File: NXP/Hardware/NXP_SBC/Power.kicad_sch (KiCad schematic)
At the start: 65 parts, among them Q1 DMN3150L-7, Q2 DMN3150L-7, Q3 DMN3150L-7, Q4 DMN3150L-7, Q5 DMN3150L-7, U3 AP3401, U4 AP3401, U5 MP2144GJ-P, U6 MAX811REUS-T

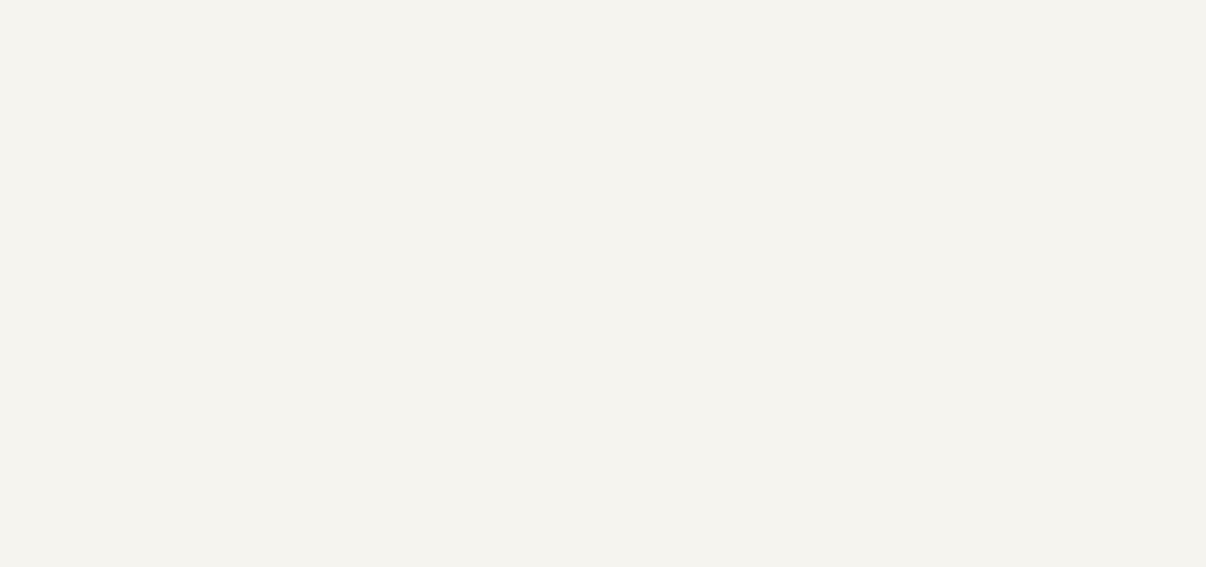
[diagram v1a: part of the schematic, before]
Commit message: Added more to ethernet schematic
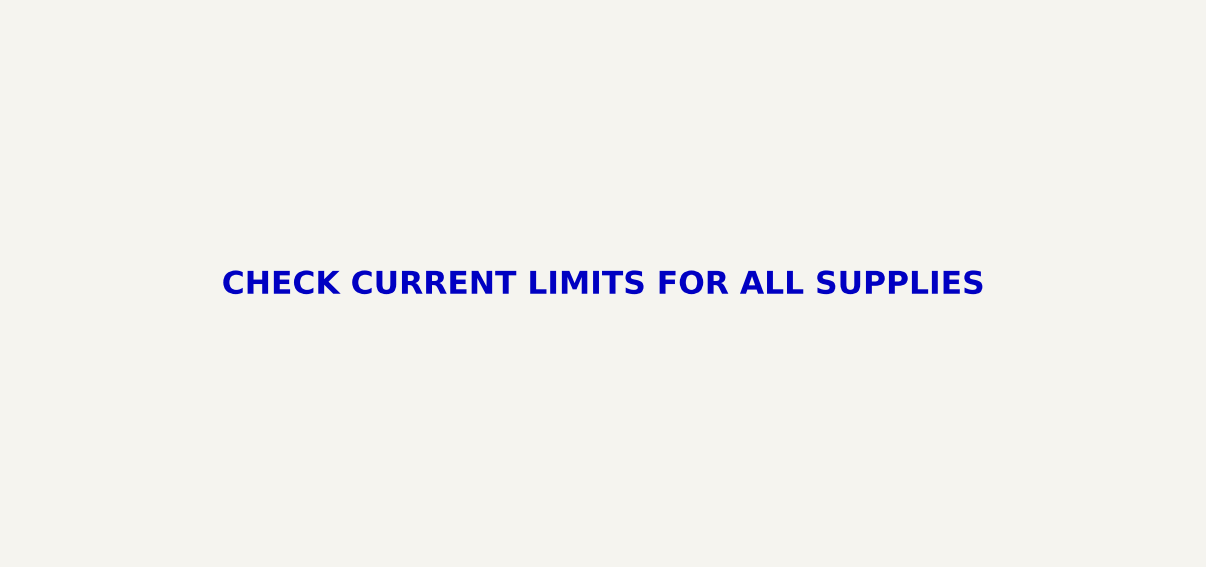
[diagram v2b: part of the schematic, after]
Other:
- note added: "CHECK CURRENT LIMITS FOR ALL SUPPLIES"
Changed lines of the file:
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@@
+		)
+	)
+	(text "CHECK CURRENT LIMITS FOR ALL SUPPLIES"
+		(exclude_from_sim no)
+		(at 196.596 302.514 0)
+		(effects
+			(font
+				(size 2.54 2.54)
+				(thickness 0.254)
+				(bold yes)
+				(color 255 0 0 1)
+			)
 		)
 	)

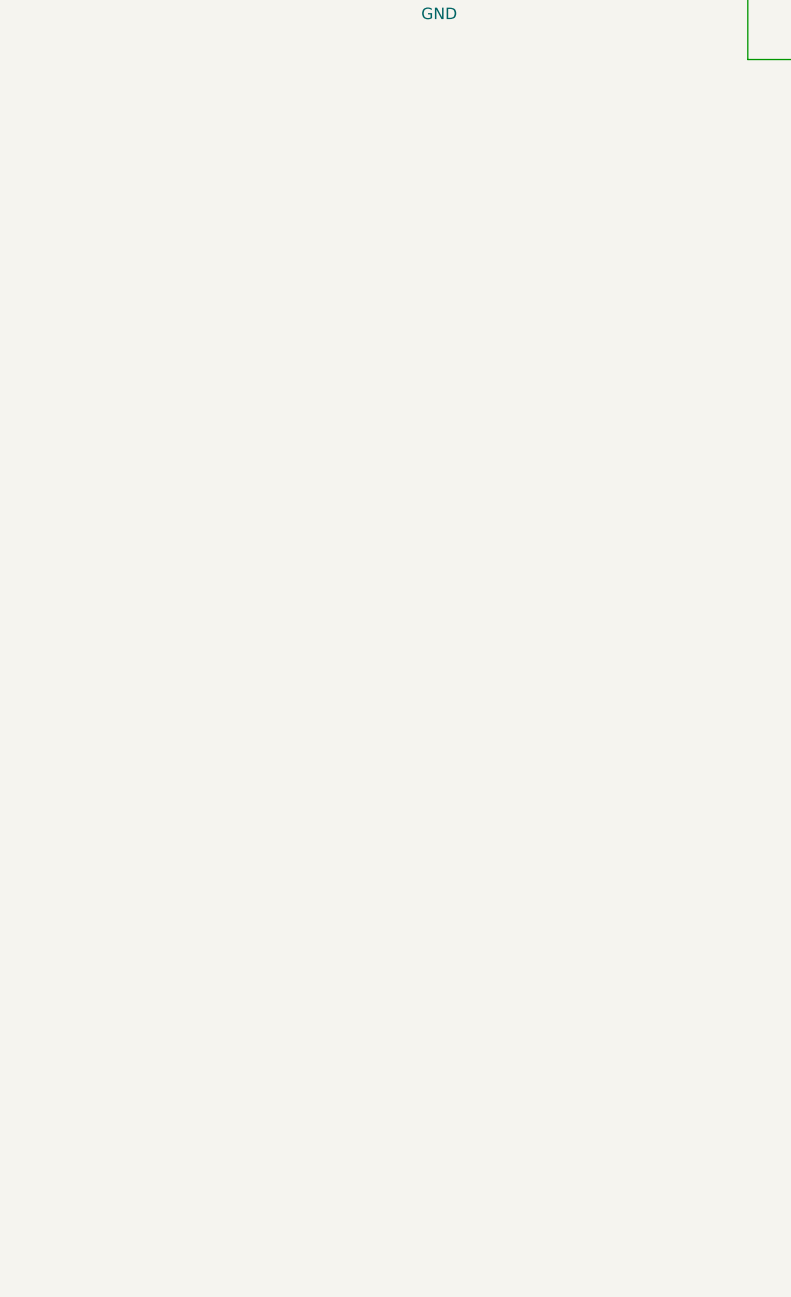
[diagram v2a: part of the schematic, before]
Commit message: added in Maya Wifi/BT module
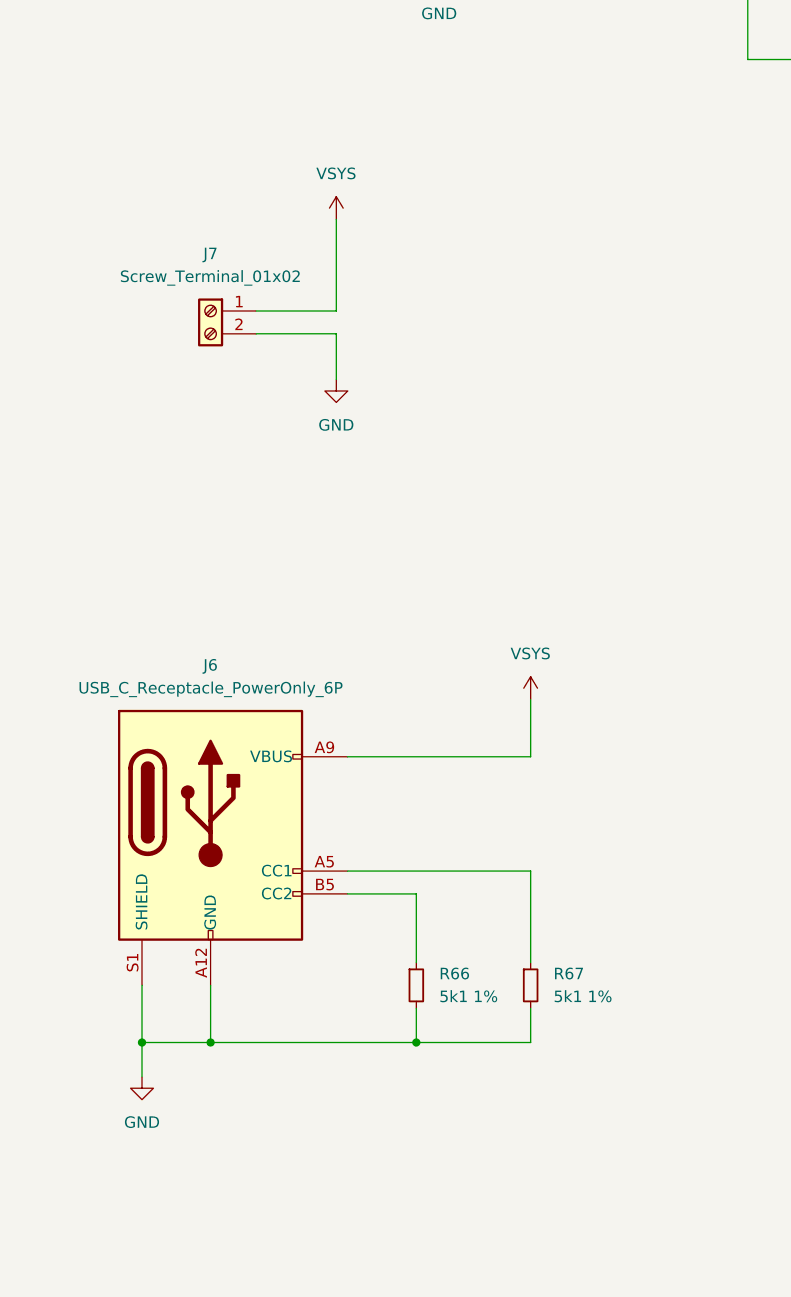
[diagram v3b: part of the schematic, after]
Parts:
- added J6: USB_C_Receptacle_PowerOnly_6P, Connector_USB:USB_C_Receptacle_GCT_USB4125-xx-x_6P_TopMnt_Horizontal, symbol Connector:USB_C_Receptacle_PowerOnly_6P
- added J7: Screw_Terminal_01x02, TerminalBlock_MetzConnect:TerminalBlock_MetzConnect_Type101_RT01602HBWC_1x02_P5.08mm_Horizontal, symbol Connector:Screw_Terminal_01x02
- added R66, R67: 5k1 1%, Resistor_SMD:R_0603_1608Metric, symbol Device:R_Small
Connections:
- net GND: now also J6.A12 (GND), J6.B12 (GND), J6.S1 (SHIELD), J7.2 (Pin_2), R66.2, R67.2
- net VSYS: now also J6.A9 (VBUS), J6.B9 (VBUS), J7.1 (Pin_1)
- new net: J6.B5 (CC2), R66.1
- new net: J6.A5 (CC1), R67.1

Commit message: More additions to schematic
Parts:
- added C61, C62: 10uF, Capacitor_SMD:C_0603_1608Metric_Pad1.08x0.95mm_HandSolder, symbol Device:C_Small
- added C63, C66: 100nF, Capacitor_SMD:C_0603_1608Metric_Pad1.08x0.95mm_HandSolder, symbol Device:C_Small
- added C64: 22pF, Capacitor_SMD:C_0603_1608Metric_Pad1.08x0.95mm_HandSolder, symbol Device:C_Small
- added C65: 22uF, Capacitor_SMD:C_0603_1608Metric_Pad1.08x0.95mm_HandSolder, symbol Device:C_Small
- added C67: 1nF, Capacitor_SMD:C_0603_1608Metric_Pad1.08x0.95mm_HandSolder, symbol Device:C_Small
- added L4: 2u2, Inductor_SMD:L_7.3x7.3_H3.5, symbol Device:L
- added Q6: DMN3150L-7, Package_TO_SOT_SMD:SOT-23, symbol Transistor_FET:DMN3150L
- added R68: 100k, Resistor_SMD:R_0603_1608Metric, symbol Device:R_Small
- added R69: 10k, Resistor_SMD:R_0603_1608Metric, symbol Device:R_Small
- added R70: 300k, 1%, Resistor_SMD:R_0603_1608Metric, symbol Device:R_Small
- added R71: 150k, 1%, Resistor_SMD:R_0603_1608Metric, symbol Device:R_Small
- added R72: 51R, Resistor_SMD:R_0603_1608Metric, symbol Device:R_Small
- added R73: 0R, Resistor_SMD:R_0603_1608Metric, symbol Device:R_Small
- added U9: AP3401, Package_TO_SOT_SMD:TSOT-23-6, symbol Regulator_Switching:AP3402
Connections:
- net DCDC_3V3: now also R69.1
- net DISCHG_EN: now also C67.1, Q6.1 (G)
- net GND: now also C61.2, C62.2, C63.2, C65.2, C66.2, C67.2, Q6.2 (S), R71.2, U9.2 (GND)
- net VSYS: now also C61.1, C62.1, C63.1, R68.1, U9.4 (VIN)
- new net: C64.2, R70.2, R71.1, U9.6 (FB)
- new net: L4.1, U9.3 (LX)
- new net: C64.1, C65.1, C66.1, L4.2, R70.1, R72.1, R73.1
- new net: R69.2, U9.1 (EN)
- new net: R68.2, U9.5 (PG)
- new net: Q6.3 (D), R72.2
- new net +1V8: R73.2
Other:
- moved on the sheet: J6, J7, R66, R67

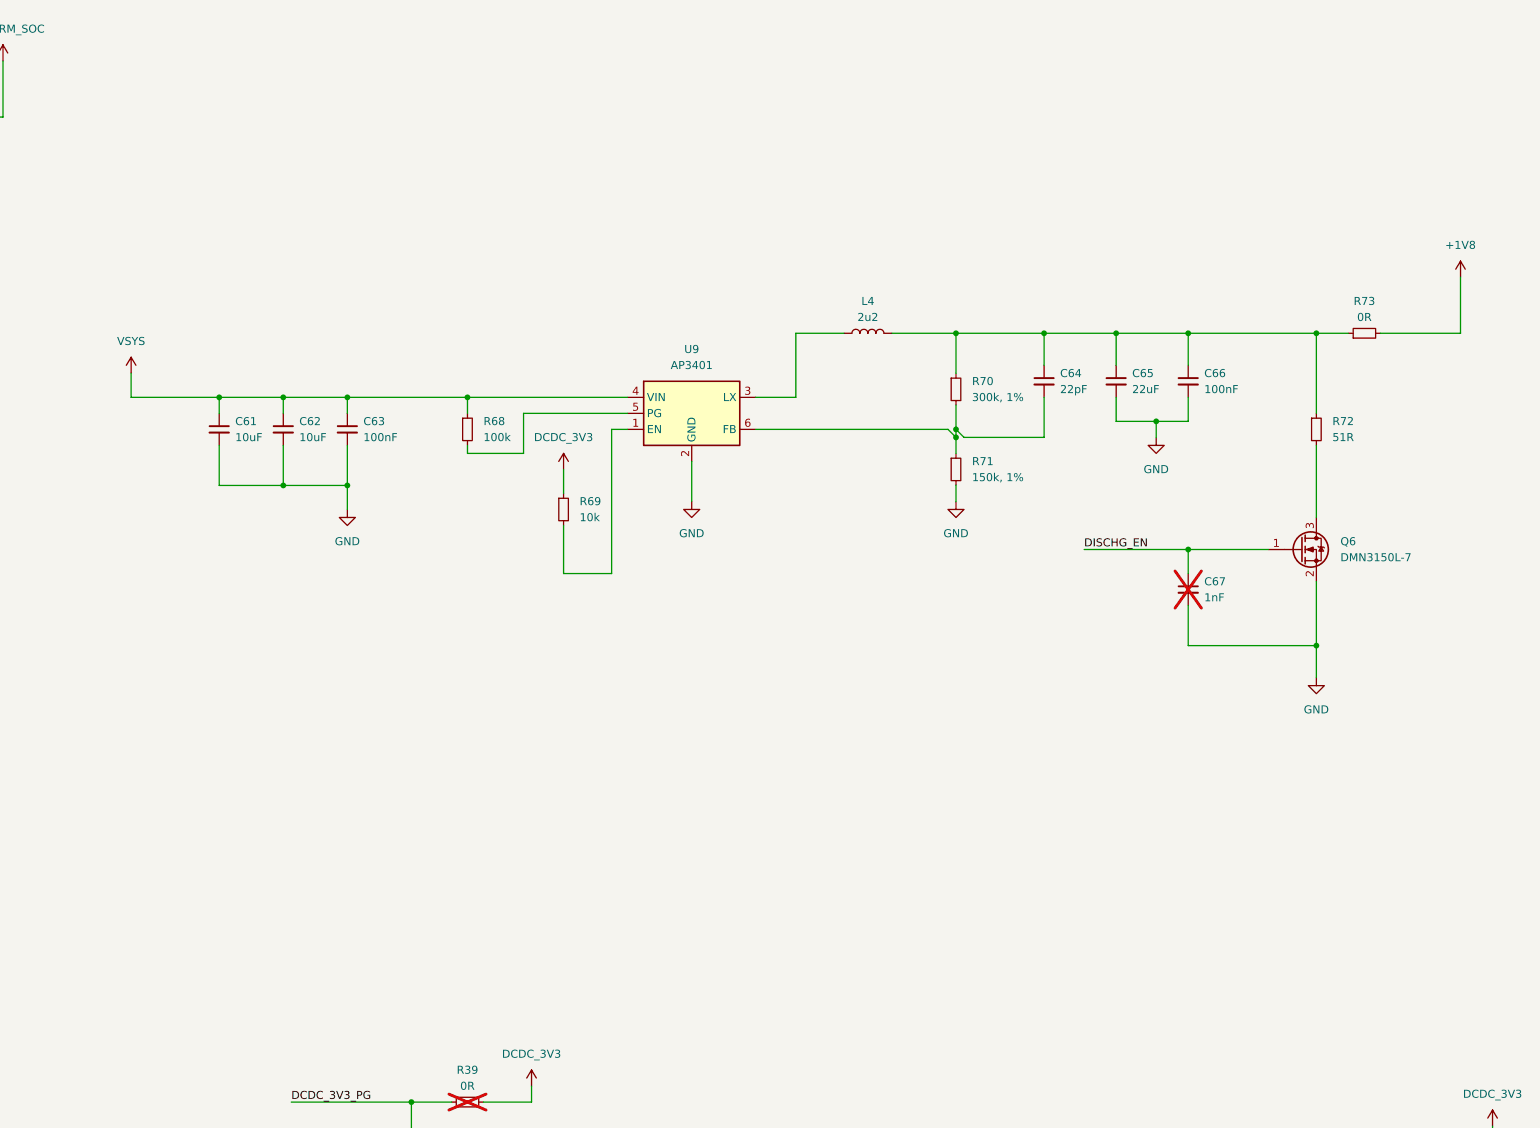
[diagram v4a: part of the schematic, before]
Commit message: Updates to radio connections
Also used the pin configurator tool to better understand pin mapping of the imx processor
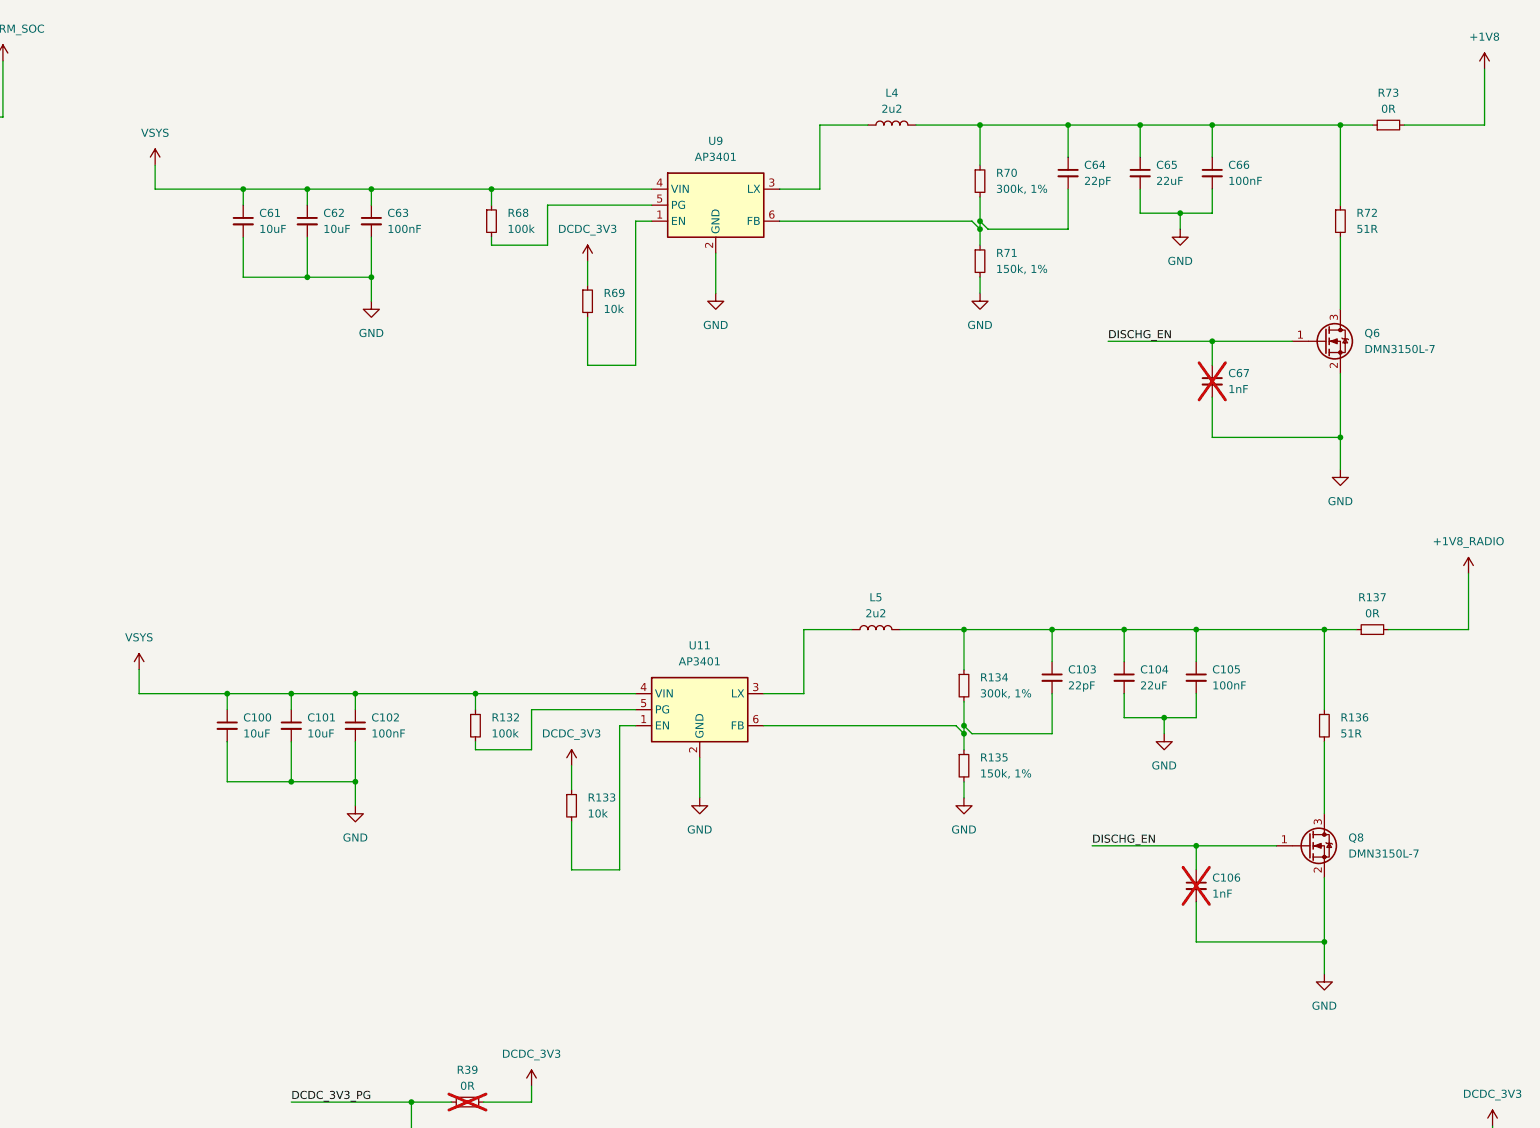
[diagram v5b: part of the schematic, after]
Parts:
- added C100, C101: 10uF, Capacitor_SMD:C_0603_1608Metric_Pad1.08x0.95mm_HandSolder, symbol Device:C_Small
- added C102, C105: 100nF, Capacitor_SMD:C_0603_1608Metric_Pad1.08x0.95mm_HandSolder, symbol Device:C_Small
- added C103: 22pF, Capacitor_SMD:C_0603_1608Metric_Pad1.08x0.95mm_HandSolder, symbol Device:C_Small
- added C104: 22uF, Capacitor_SMD:C_0603_1608Metric_Pad1.08x0.95mm_HandSolder, symbol Device:C_Small
- added C106: 1nF, Capacitor_SMD:C_0603_1608Metric_Pad1.08x0.95mm_HandSolder, symbol Device:C_Small
- added L5: 2u2, Inductor_SMD:L_7.3x7.3_H3.5, symbol Device:L
- added Q8: DMN3150L-7, Package_TO_SOT_SMD:SOT-23, symbol Transistor_FET:DMN3150L
- added R132: 100k, Resistor_SMD:R_0603_1608Metric, symbol Device:R_Small
- added R133: 10k, Resistor_SMD:R_0603_1608Metric, symbol Device:R_Small
- added R134: 300k, 1%, Resistor_SMD:R_0603_1608Metric, symbol Device:R_Small
- added R135: 150k, 1%, Resistor_SMD:R_0603_1608Metric, symbol Device:R_Small
- added R136: 51R, Resistor_SMD:R_0603_1608Metric, symbol Device:R_Small
- added R137: 0R, Resistor_SMD:R_0603_1608Metric, symbol Device:R_Small
- added U11: AP3401, Package_TO_SOT_SMD:TSOT-23-6, symbol Regulator_Switching:AP3402
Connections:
- net DCDC_3V3: now also R133.1
- net DISCHG_EN: now also C106.1, Q8.1 (G)
- net GND: now also C100.2, C101.2, C102.2, C104.2, C105.2, C106.2, Q8.2 (S), R135.2, U11.2 (GND)
- net VSYS: now also C100.1, C101.1, C102.1, R132.1, U11.4 (VIN)
- new net: C103.1, C104.1, C105.1, L5.2, R134.1, R136.1, R137.1
- new net: R133.2, U11.1 (EN)
- new net: L5.1, U11.3 (LX)
- new net: R132.2, U11.5 (PG)
- new net: C103.2, R134.2, R135.1, U11.6 (FB)
- new net: Q8.3 (D), R136.2
- new net +1V8_RADIO: R137.2
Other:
- moved on the sheet: C61, C62, C63, C64, C65, C66, C67, L4, Q6, R68, R69, R70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
